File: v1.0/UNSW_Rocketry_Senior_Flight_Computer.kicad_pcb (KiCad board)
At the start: 4 copper layers, 80 x 50 mm, 129 parts, among them J1 SWD, J10 J_BATT, J2 Micro_SD_Card_Det1, J3 USB_C_Receptacle_USB2.0_16P, J5 Conn_01x04, J7 J_PYRO1, J8 J_PYRO2, J9 J_PYRO_BAT, Q1 DMG2301L, Q2 AO3401A, Q3 AO3400A, Q4 AO3400A, Q5 AO3400A, U1 STM32L452RETx, U10 PC817, U11 PC817, U2 TPS63060, U3 SPX3819M5-L-3-3, U4 H3LIS331DL, U5 MS5611 #1, U6 LIS3DH, U7 MS5611 #2, U8 USBLC6-2SC6, U9 PC817, Y1 8MHz

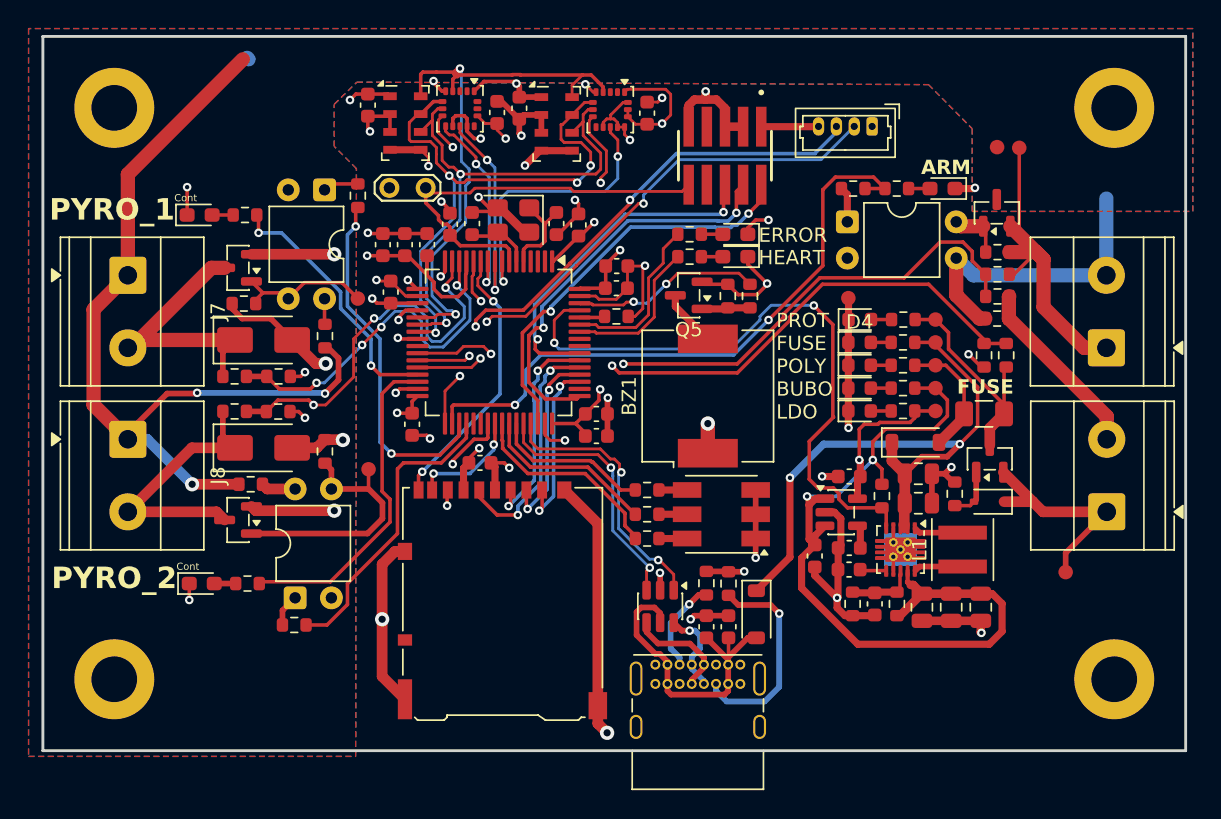
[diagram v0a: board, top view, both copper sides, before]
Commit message: v1.0: update Power/Pyros schematics and PCB; add JUNO_XL and Untitled_2 footprints
Co-Authored-By: Claude Opus 4.8 (1M context) <noreply@anthropic.com>
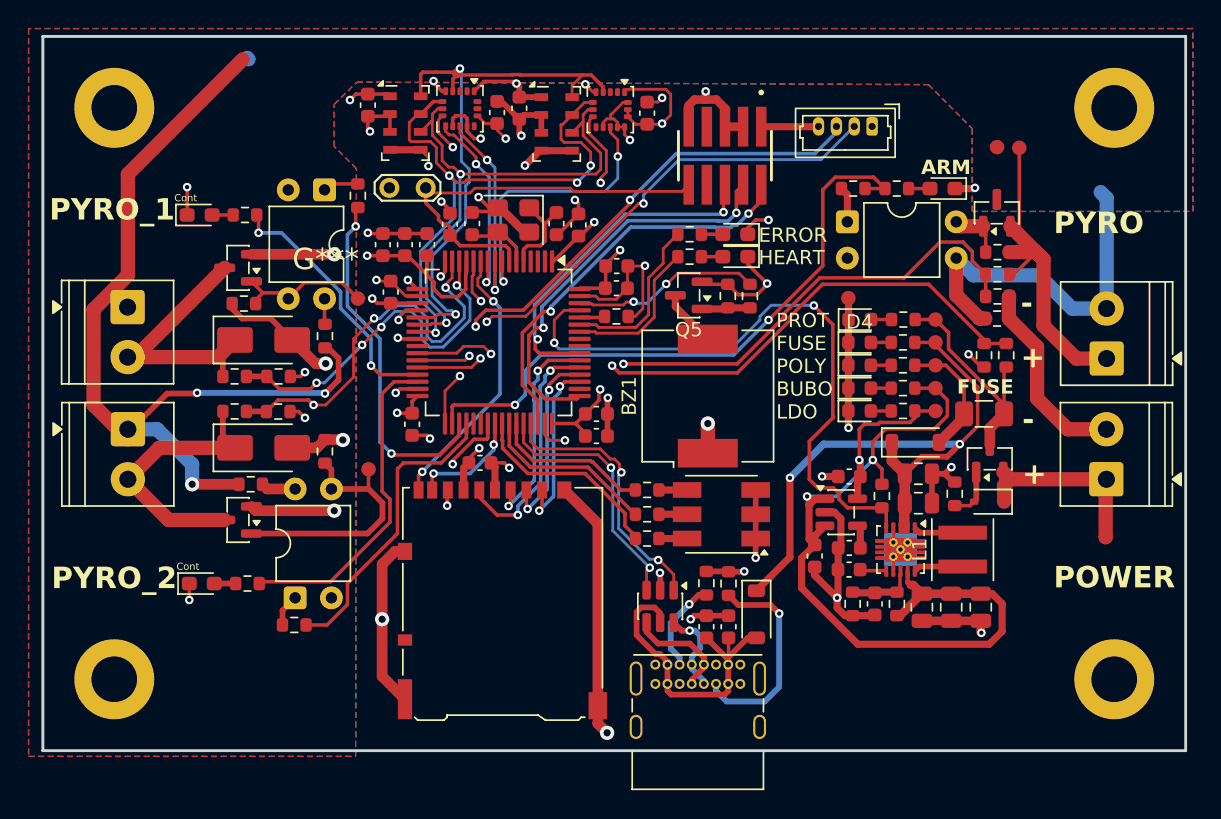
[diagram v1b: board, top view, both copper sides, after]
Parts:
- added G***: Juno_Wide, UNSW_ROCKETRY_LIBRARY:JUNO_XL, F.Cu at (138.2, 104.5)
- added G***: LOGO, UNSW_ROCKETRY_LIBRARY:ROCKETRY_LOGO_LARGE, F.Cu at (132.4, 89.7)
- J10, J7, J8, J9: footprint TerminalBlock_Phoenix:TerminalBlock_Phoenix_MKDS-1,5-2-5.08_1x02_P5.08mm_Horizontal -> TerminalBlock_Phoenix:TerminalBlock_Phoenix_PT-1,5-2-3.5-H_1x02_P3.50mm_Horizontal
- moved TP1 3.72 mm to (187.0, 109.2)
- moved J10 2.28 mm to (187.1, 105.2)
- moved J7 2.23 mm to (118.5, 93.1)
- moved J9 0.75 mm to (187.1, 96.7)
- moved J8 0.70 mm to (118.5, 101.7)
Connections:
- H1 pad 1: GND -> (no net)
- H2 pad 1: GND -> (no net)
- H3 pad 1: GND -> (no net)
- H4 pad 1: GND -> (no net)
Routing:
- net PYRO_GND: track 45.8 -> 49.8 mm
- net VBAT_RAW: track 16.2 -> 13.3 mm
- net PYRO_BATT: track 61.1 -> 62.2 mm
- net PYRO_BATT_RAW: track 25.1 -> 26.2 mm
- net GND: track 181.9 -> 182.8 mm
- net Net-(D11-A1): track 19.7 -> 20.5 mm
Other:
- board text added: "+"
- board text added: "-"
- board text added: "BY DASHIELL RUSSELL"
- board text added: "POWER"
- board text added: "PROJECT OZONE"
- board text added: "PYRO"
- board text added: "UNSW ROCKETRY SENIOR FLIGHT COMPUTER"
